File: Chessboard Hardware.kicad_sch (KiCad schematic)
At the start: 0 parts

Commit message: Finish settings
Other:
- title: (none) -> Chessboard Hardware
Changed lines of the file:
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@@
 	(paper "USLetter")
 	(title_block
+		(title "Chessboard Hardware")
 		(rev "1")
 	)

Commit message: Schematic done
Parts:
- added A1: Arduino_Nano_v3.x, Module:Arduino_Nano, symbol MCU_Module:Arduino_Nano_v3.x
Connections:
- new net COM0: A1.19 (A0)
- new net COM1: A1.20 (A1)
- new net COM2: A1.21 (A2)
- new net COM3: A1.22 (A3)
- new net EN: A1.9 (D6)
- new net GND: A1.29 (GND), A1.4 (GND)
- new net S0: A1.5 (D2)
- new net S1: A1.6 (D3)
- new net S2: A1.7 (D4)
- new net S3: A1.8 (D5)
- new net VCC: A1.27 (+5V)
- no-connect marks 0 -> 18
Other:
- added sheet Bottom left sensor quarter (Sensor Quarter.kicad_sch)
- added sheet Bottom right sensor quarter (Sensor Quarter.kicad_sch)
- added sheet Top left sensor quarter (Sensor Quarter.kicad_sch)
- added sheet Top right sensor quarter (Sensor Quarter.kicad_sch)

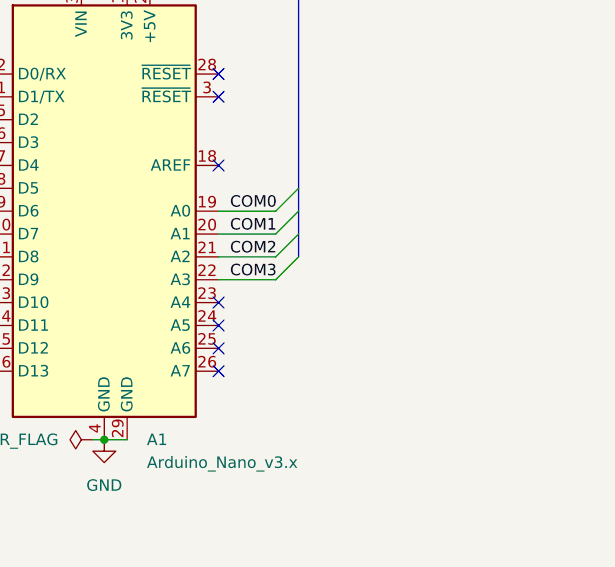
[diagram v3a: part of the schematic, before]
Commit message: Silkscreen lines for center of chess squares on PCB
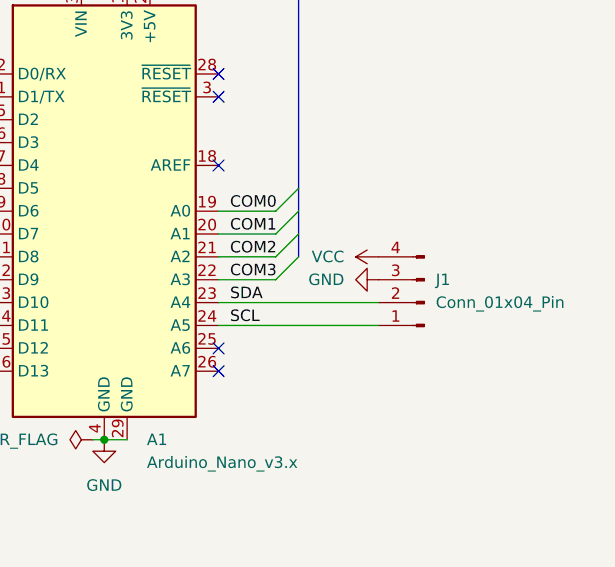
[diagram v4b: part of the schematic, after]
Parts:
- added J1: Conn_01x04_Pin, Connector_PinHeader_2.54mm:PinHeader_1x04_P2.54mm_Vertical, symbol Connector:Conn_01x04_Pin
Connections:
- net GND: now also J1.3 (Pin_3)
- net VCC: now also J1.4 (Pin_4)
- net SDA: now reaches A1.23 (A4)
- net SDA: now also J1.2 (Pin_2)
- net SCL: now reaches A1.24 (A5)
- net SCL: now also J1.1 (Pin_1)
- no-connect marks 18 -> 16
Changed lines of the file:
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@@
-	)
-	(no_connect
-		(at 114.3 111.76)
 	)
 	(no_connect
@@
 	)
 	(no_connect
-		(at 114.3 109.22)
-	)
-	(no_connect
 		(at 114.3 83.82)
 	)
@@
 	(wire
 		(pts
+			(xy 114.3 111.76) (xy 132.08 111.76)
+		)
+		(stroke
+			(width 0)
+			(type default)
+		)
+	)
+	(wire
+		(pts
 			(xy 69.85 121.92) (xy 76.2 121.92)
 		)
@@
 		(pts
 			(xy 114.3 101.6) (xy 120.65 101.6)
+		)
+		(stroke
+			(width 0)
+			(type default)
+		)
+	)
+	(wire
+		(pts
+			(xy 114.3 109.22) (xy 132.08 109.22)
 		)
 		(stroke
@@
 	(label "S0"
 		(at 73.66 167.64 0)
+		(effects
+			(font
+				(size 1.27 1.27)
+			)
+			(justify left bottom)
+		)
+	)
+	(label "SCL"
+		(at 115.57 111.76 0)
+		(effects
+			(font
+				(size 1.27 1.27)
+			)
+			(justify left bottom)
+		)
+	)
+	(label "SDA"
+		(at 115.57 109.22 0)
 		(effects
 			(font
@@
 	)
 	(symbol
+		(lib_id "Connector:Conn_01x04_Pin")
+		(at 137.16 109.22 180)
+		(unit 1)
+		(exclude_from_sim no)
+		(in_bom yes)
+		(on_board yes)
+		(dnp no)
+		(fields_autoplaced yes)
+		(property "Reference" "J1"
+			(at 138.43 106.6799 0)
+			(effects
+				(font
+					(size 1.27 1.27)
+				)
+				(justify right)
+			)
+		)
+		(property "Value" "Conn_01x04_Pin"
+			(at 138.43 109.2199 0)
+			(effects
+				(font
+					(size 1.27 1.27)
+				)
+				(justify right)
+			)
+		)
+		(property "Footprint" "Connector_PinHeader_2.54mm:PinHeader_1x04_P2.54mm_Vertical"
+			(at 137.16 109.22 0)
+			(effects
+				(font
+					(size 1.27 1.27)
+				)
+				(hide yes)
+			)
+		)
+		(property "Datasheet" "~"
+			(at 137.16 109.22 0)
+			(effects
+				(font
+					(size 1.27 1.27)
+				)
+				(hide yes)
+			)
+		)
+		(property "Description" "Generic connector, single row, 01x04, script generated"
+			(at 137.16 109.22 0)
+			(effects
+				(font
+					(size 1.27 1.27)
+				)
+				(hide yes)
+			)
+		)
+		(pin "3"
+		)
+		(pin "4"
+		)
+		(pin "1"
+		)
+		(pin "2"
+		)
+		(instances
+			(project ""
+				(path "/e63e39d7-6ac0-4ffd-8aa3-1841a4541b55"
+					(reference "J1")
+					(unit 1)
+				)
+			)
+		)
+	)
+	(symbol
+		(lib_id "power:GND")
+		(at 132.08 106.68 270)
+		(unit 1)
+		(exclude_from_sim no)
+		(in_bom yes)
+		(on_board yes)
+		(dnp no)
+		(fields_autoplaced yes)
+		(property "Reference" "#PWR0144"
+			(at 125.73 106.68 0)
+			(effects
+				(font
+					(size 1.27 1.27)
+				)
+				(hide yes)
+			)
+		)
+		(property "Value" "GND"
+			(at 128.27 106.6799 90)
+			(effects
+				(font
+					(size 1.27 1.27)
+				)
+				(justify right)
+			)
+		)
+		(property "Footprint" ""
+			(at 132.08 106.68 0)
+			(effects
+				(font
+					(size 1.27 1.27)
+				)
+				(hide yes)
+			)
+		)
+		(property "Datasheet" ""
+			(at 132.08 106.68 0)
+			(effects
+				(font
+					(size 1.27 1.27)
+				)
+				(hide yes)
+			)
+		)
+		(property "Description" "Power symbol creates a global label with name \"GND\" , ground"
+			(at 132.08 106.68 0)
+			(effects
+				(font
+					(size 1.27 1.27)
+				)
+				(hide yes)
+			)
+		)
+		(pin "1"
+		)
+		(instances
+			(project ""
+				(path "/e63e39d7-6ac0-4ffd-8aa3-1841a4541b55"
+					(reference "#PWR0144")
+					(unit 1)
+				)
+			)
+		)
+	)
+	(symbol
 		(lib_id "power:VCC")
 		(at 106.68 73.66 0)
@@
 					(unit 1)
 				)
+			)
+		)
+	)
+	(symbol
+		(lib_id "power:VCC")
+		(at 132.08 104.14 90)
+		(unit 1)
+		(exclude_from_sim no)
+		(in_bom yes)
+		(on_board yes)
+		(dnp no)
+		(fields_autoplaced yes)
+		(property "Reference" "#PWR0143"
+			(at 135.89 104.14 0)
+			(effects
+				(font
+					(size 1.27 1.27)
+				)
+				(hide yes)
+			)
+		)
+		(property "Value" "VCC"
+			(at 128.27 104.1399 90)
+			(effects
+				(font
+					(size 1.27 1.27)
+				)
+				(justify left)
+			)
+		)
+		(property "Footprint" ""
+			(at 132.08 104.14 0)
+			(effects
+				(font
+					(size 1.27 1.27)
+				)
+				(hide yes)
+			)
+		)
+		(property "Datasheet" ""
+			(at 132.08 104.14 0)
+			(effects
+				(font
+					(size 1.27 1.27)
+				)
+				(hide yes)
+			)
+		)
+		(property "Description" "Power symbol creates a global label with name \"VCC\""
+			(at 132.08 104.14 0)
+			(effects
+				(font
+					(size 1.27 1.27)
+				)
+				(hide yes)
+			)
+		)
+		(pin "1"
+		)
+		(instances
+			(project ""
+				(path "/e63e39d7-6ac0-4ffd-8aa3-1841a4541b55"
+					(reference "#PWR0143")
+					(unit 1)
+				)

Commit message: Done and Gerbers
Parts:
- added TP1, TP10, TP11, TP2, TP3, TP4, TP5, TP6, TP7, TP8, TP9: TestPoint, SamacSys_PCB_Library_KiCad:TestPoint, symbol Connector:TestPoint
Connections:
- net COM0: now also TP8.1
- net COM1: now also TP7.1
- net COM2: now also TP6.1
- net COM3: now also TP5.1
- net EN: now also TP9.1
- net GND: now also TP11.1
- net S0: now also TP4.1
- net S1: now also TP3.1
- net S2: now also TP2.1
- net S3: now also TP1.1
- net VCC: now also TP10.1

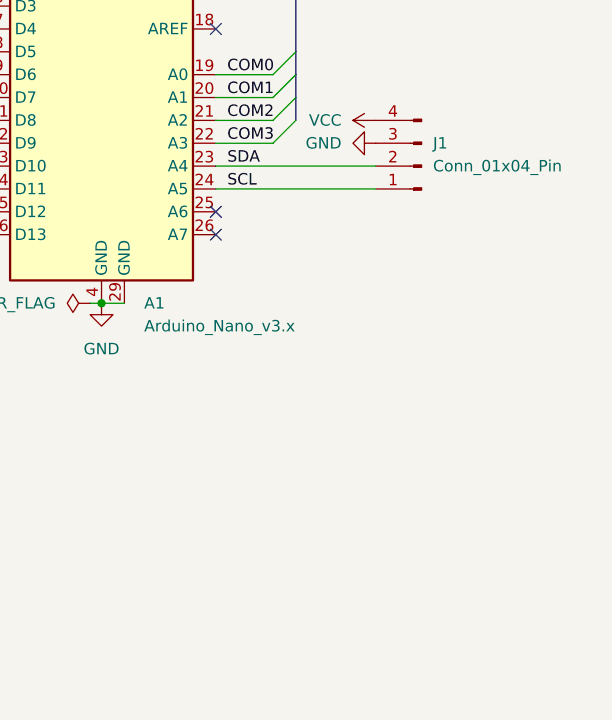
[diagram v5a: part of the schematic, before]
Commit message: Add 4 pin header to all sides for convenience
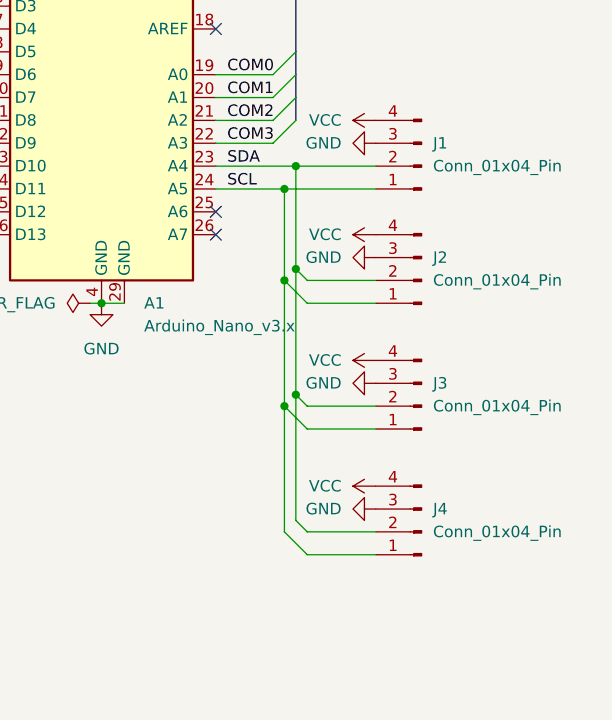
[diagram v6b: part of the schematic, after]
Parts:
- added J2, J3, J4: Conn_01x04_Pin, Connector_PinHeader_2.54mm:PinHeader_1x04_P2.54mm_Vertical, symbol Connector:Conn_01x04_Pin
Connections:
- net GND: now also J2.3 (Pin_3), J3.3 (Pin_3), J4.3 (Pin_3)
- net SCL: now also J2.1 (Pin_1), J3.1 (Pin_1), J4.1 (Pin_1)
- net SDA: now also J2.2 (Pin_2), J3.2 (Pin_2), J4.2 (Pin_2)
- net VCC: now also J2.4 (Pin_4), J3.4 (Pin_4), J4.4 (Pin_4)

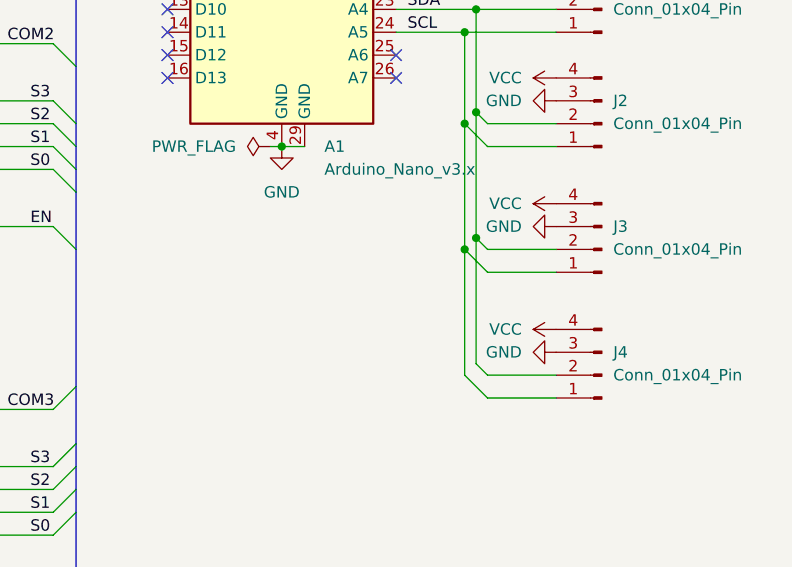
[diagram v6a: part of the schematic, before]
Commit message: I2C pull ups
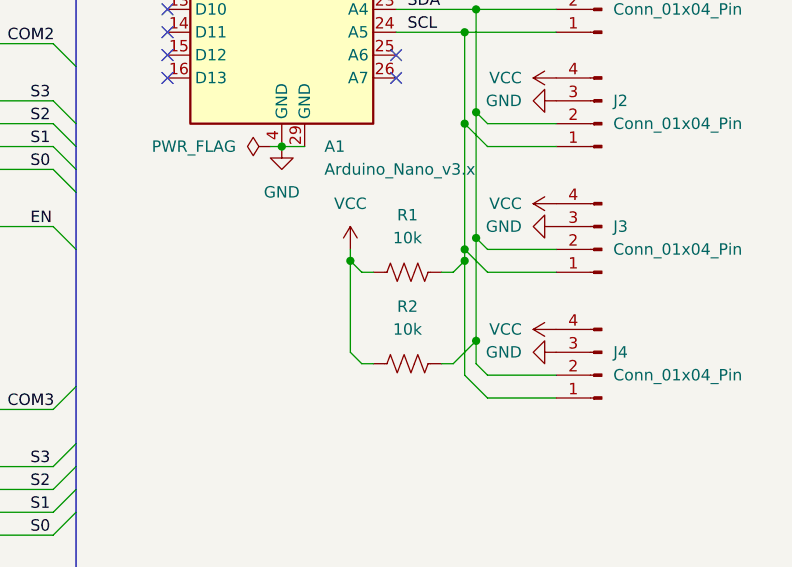
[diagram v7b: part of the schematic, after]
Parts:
- added R1, R2: 10k, Resistor_THT:R_Axial_DIN0207_L6.3mm_D2.5mm_P10.16mm_Horizontal, symbol Device:R_US
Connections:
- net SCL: now also R1.2
- net SDA: now also R2.2
- net VCC: now also R1.1, R2.1

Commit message: Cleanup
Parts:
- removed J2, J3, J4: Conn_01x04_Pin, Connector_PinHeader_2.54mm:PinHeader_1x04_P2.54mm_Vertical, symbol Connector:Conn_01x04_Pin
